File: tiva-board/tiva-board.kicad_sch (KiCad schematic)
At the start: 28 parts, among them J1 Printstecker_1x03, J2 Printstecker_1x03, J3 Printstecker_1x02, J4 Printstecker_1x02, J5 Printstecker_1x02, J6 Printstecker_1x04, J7 Conn_01x04_Socket, U1 NJM4556A

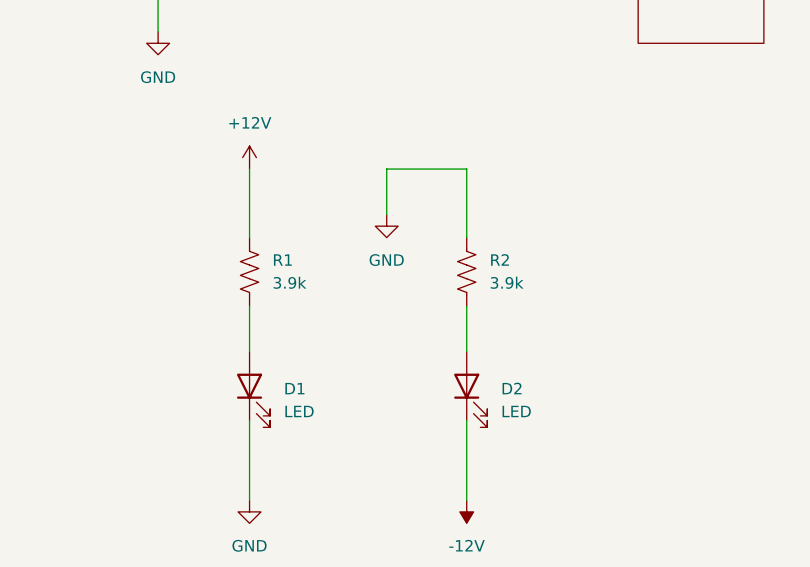
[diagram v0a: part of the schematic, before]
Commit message: Updated resistor values on the Tiva board
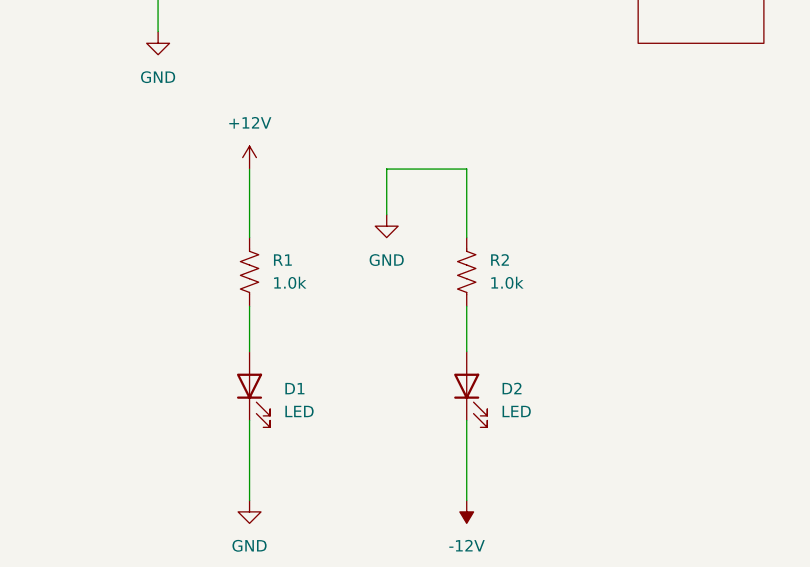
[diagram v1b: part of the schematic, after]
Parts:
- R1, R2: value 3.9k -> 1.0k
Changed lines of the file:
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@@
       (effects (font (size 1.27 1.27)) (justify left))
     )
-    (property "Value" "3.9k" (at 132.08 138.43 0)
+    (property "Value" "1.0k" (at 132.08 138.43 0)
       (effects (font (size 1.27 1.27)) (justify left))
     )
@@
       (effects (font (size 1.27 1.27)) (justify left))
     )
-    (property "Value" "3.9k" (at 156.21 138.43 0)
-      (effects (font (size 1.27 1.27)) (justify left))
-    )
+    (property "Value" "1.0k" (at 156.21 138.43 0)
+      (effects (font (size 1.27 1.27)) (justify left))
+    )
